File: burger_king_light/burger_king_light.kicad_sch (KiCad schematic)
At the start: 1 part, among them J1 Jack-DC

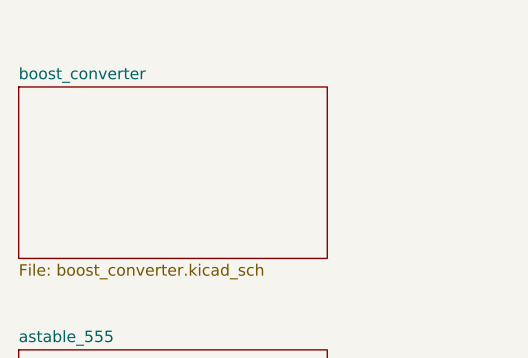
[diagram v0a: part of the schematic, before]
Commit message: renamed sheet
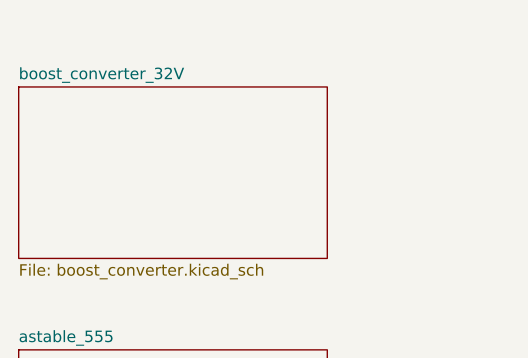
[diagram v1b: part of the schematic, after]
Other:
- sheet boost_converter renamed boost_converter_32V
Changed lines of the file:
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@@
 			(color 0 0 0 0)
 		)
-		(property "Sheetname" "boost_converter"
+		(property "Sheetname" "boost_converter_32V"
 			(at 58.42 38.6584 0)
 			(show_name no)

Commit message: renamed sheet. wip.
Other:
- sheet boost_converter_32V renamed boost_converter_36V
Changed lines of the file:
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@@
 			(color 0 0 0 0)
 		)
-		(property "Sheetname" "boost_converter_32V"
+		(property "Sheetname" "boost_converter_36V"
 			(at 58.42 38.6584 0)
 			(show_name no)

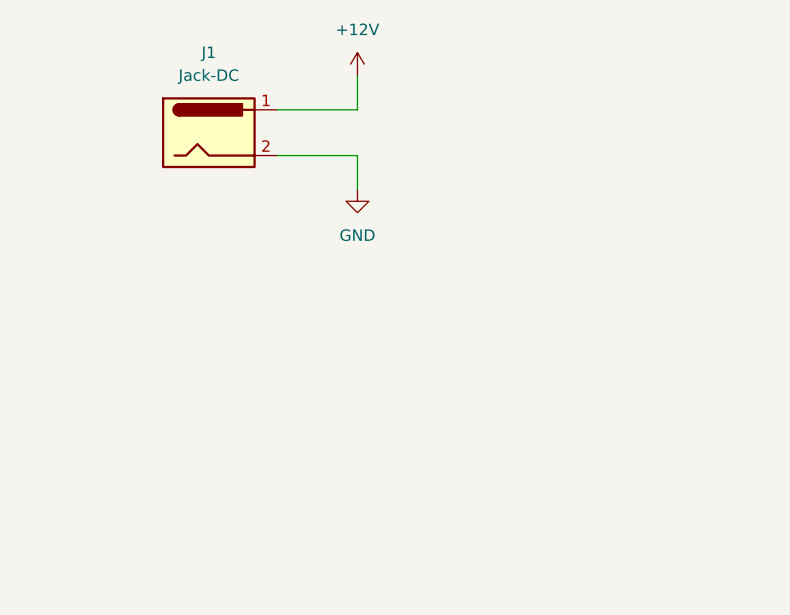
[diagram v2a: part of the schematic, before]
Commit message: reduced mounting hole size
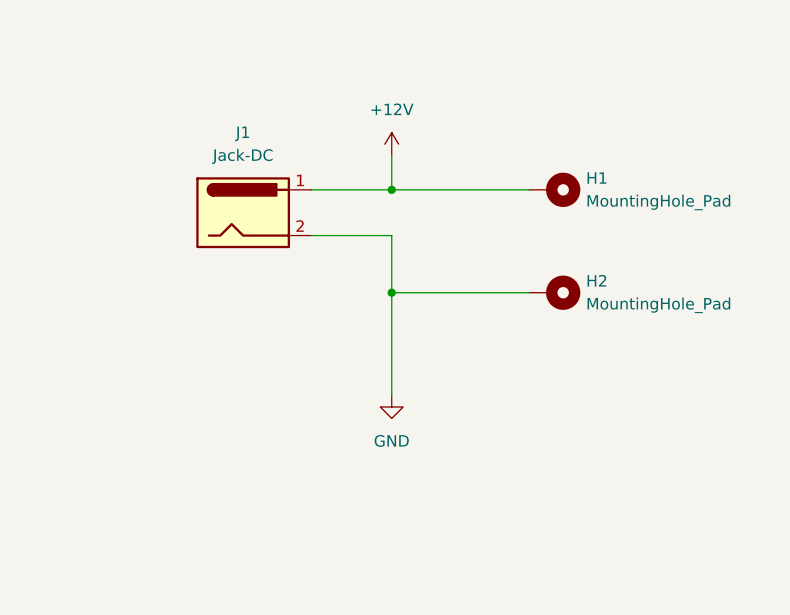
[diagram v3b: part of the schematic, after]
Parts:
- added H1, H2: MountingHole_Pad, MountingHole:MountingHole_3.5mm_Pad_TopBottom, symbol Mechanical:MountingHole_Pad
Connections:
- net +12V: now also H1.1
- net GND: now also H2.1
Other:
- moved on the sheet: J1
